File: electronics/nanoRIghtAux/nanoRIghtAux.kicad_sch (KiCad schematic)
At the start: 18 parts, among them J1 Conn_MM5451, J10 Conn_EA_GLCD, J11 Conn_MAX7219, J12 Conn_PWRInput, J13 Conn_MAX_Pwr, J2 Conn_HYDA, J3 Conn_HYDB, J4 Conn_FUEL_FR, J5 Conn_FUEL_AL, J6 Conn_MOT_D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

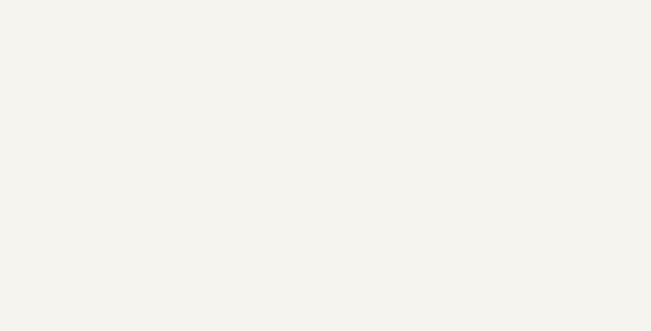
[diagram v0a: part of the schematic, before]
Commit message: mountingholes addes
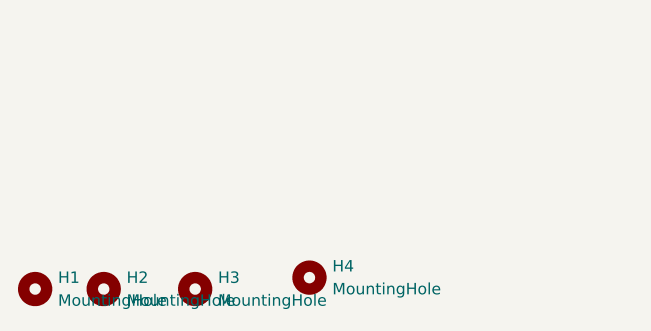
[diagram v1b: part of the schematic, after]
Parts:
- added H1, H2, H3, H4: MountingHole, MountingHole:MountingHole_3.5mm, symbol Mechanical:MountingHole
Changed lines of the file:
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@@
     (effects (font (size 1.27 1.27)) (justify left bottom))
+  )
+  (symbol (lib_id "Mechanical:MountingHole") (at 39.37 187.96 0) (unit 1)
+    (in_bom yes) (on_board yes) (dnp no) (fields_autoplaced)
+    (property "Reference" "H3" (at 41.91 186.69 0)
+      (effects (font (size 1.27 1.27)) (justify left))
+    )
+    (property "Value" "MountingHole" (at 41.91 189.23 0)
+      (effects (font (size 1.27 1.27)) (justify left))
+    )
+    (property "Footprint" "MountingHole:MountingHole_3.5mm" (at 39.37 187.96 0)
+      (effects (font (size 1.27 1.27)) hide)
+    )
+    (property "Datasheet" "~" (at 39.37 187.96 0)
+      (effects (font (size 1.27 1.27)) hide)
+    )
+    (instances
+      (project "nanoRIghtAux"
+        (path "/36bd7c2a-95a7-4ab3-af81-512b588298f0"
+          (reference "H3") (unit 1)
+        )
+      )
+    )
   )
   (symbol (lib_id "power:+5V") (at 90.17 121.92 0) (mirror x) (unit 1)
@@
         (path "/36bd7c2a-95a7-4ab3-af81-512b588298f0"
           (reference "SW2") (unit 1)
+        )
+      )
+    )
+  )
+  (symbol (lib_id "Mechanical:MountingHole") (at 29.21 187.96 0) (unit 1)
+    (in_bom yes) (on_board yes) (dnp no) (fields_autoplaced)
+    (property "Reference" "H2" (at 31.75 186.69 0)
+      (effects (font (size 1.27 1.27)) (justify left))
+    )
+    (property "Value" "MountingHole" (at 31.75 189.23 0)
+      (effects (font (size 1.27 1.27)) (justify left))
+    )
+    (property "Footprint" "MountingHole:MountingHole_3.5mm" (at 29.21 187.96 0)
+      (effects (font (size 1.27 1.27)) hide)
+    )
+    (property "Datasheet" "~" (at 29.21 187.96 0)
+      (effects (font (size 1.27 1.27)) hide)
+    )
+    (instances
+      (project "nanoRIghtAux"
+        (path "/36bd7c2a-95a7-4ab3-af81-512b588298f0"
+          (reference "H2") (unit 1)
         )
       )
@@
         )
       )
+    )
+  )
+  (symbol (lib_id "Mechanical:MountingHole") (at 52.07 186.69 0) (unit 1)
+    (in_bom yes) (on_board yes) (dnp no) (fields_autoplaced)
+    (property "Reference" "H4" (at 54.61 185.42 0)
+      (effects (font (size 1.27 1.27)) (justify left))
+    )
+    (property "Value" "MountingHole" (at 54.61 187.96 0)
+      (effects (font (size 1.27 1.27)) (justify left))
+    )
+    (property "Footprint" "MountingHole:MountingHole_3.5mm" (at 52.07 186.69 0)
+      (effects (font (size 1.27 1.27)) hide)
+    )
+    (property "Datasheet" "~" (at 52.07 186.69 0)
+      (effects (font (size 1.27 1.27)) hide)
+    )
+    (instances
+      (project "nanoRIghtAux"
+        (path "/36bd7c2a-95a7-4ab3-af81-512b588298f0"
+          (reference "H4") (unit 1)
+        )
+      )
+    )
+  )
+  (symbol (lib_id "Mechanical:MountingHole") (at 21.59 187.96 0) (unit 1)
+    (in_bom yes) (on_board yes) (dnp no) (fields_autoplaced)
+    (property "Reference" "H1" (at 24.13 186.69 0)
+      (effects (font (size 1.27 1.27)) (justify left))
+    )
+    (property "Value" "MountingHole" (at 24.13 189.23 0)
+      (effects (font (size 1.27 1.27)) (justify left))
+    )
+    (property "Footprint" "MountingHole:MountingHole_3.5mm" (at 21.59 187.96 0)
+      (effects (font (size 1.27 1.27)) hide)
+    )
+    (property "Datasheet" "~" (at 21.59 187.96 0)
+      (effects (font (size 1.27 1.27)) hide)
+    )
+    (instances
+      (project "nanoRIghtAux"
+        (path "/36bd7c2a-95a7-4ab3-af81-512b588298f0"
+          (reference "H1") (unit 1)
+        )
+      )

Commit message: changed footprint of AX12 to DIP28
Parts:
- U3: footprint Package_SO:SOIC-28W_7.5x17.9mm_P1.27mm -> Package_DIP:DIP-28_W15.24mm
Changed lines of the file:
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@@
       (effects (font (size 1.27 1.27)) (justify left))
     )
-    (property "Footprint" "Package_SO:SOIC-28W_7.5x17.9mm_P1.27mm" (at 220.98 96.52 0)
+    (property "Footprint" "Package_DIP:DIP-28_W15.24mm" (at 220.98 96.52 0)
       (effects (font (size 1.27 1.27)) hide)
     )

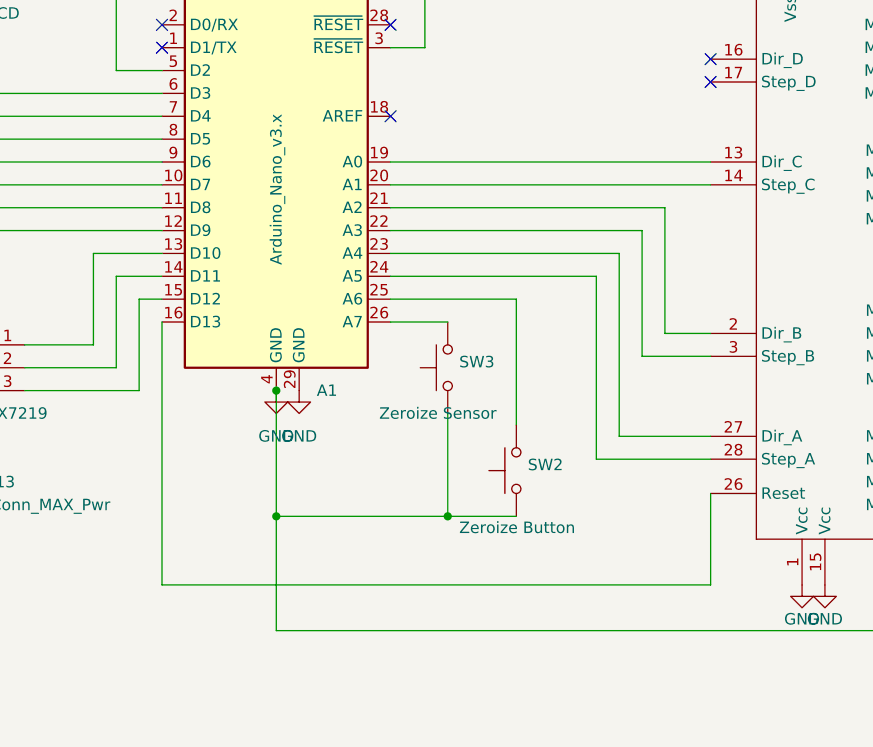
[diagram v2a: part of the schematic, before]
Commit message: changed pin assignments for AX12 to facilitate routing
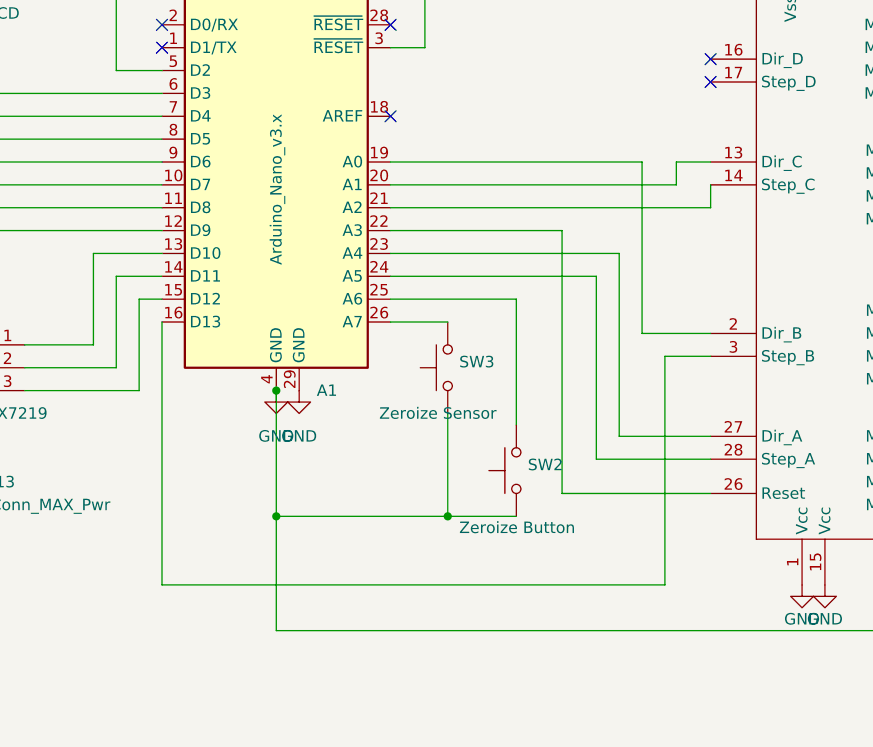
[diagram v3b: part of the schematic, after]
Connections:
- net at U3.13 (Dir_C): now also A1.20 (A1); no longer A1.19 (A0)
- net at U3.14 (Step_C): now also A1.21 (A2); no longer A1.20 (A1)
- net at U3.2 (Dir_B): now also A1.19 (A0); no longer A1.21 (A2)
- net at U3.26 (Reset): now also A1.22 (A3); no longer A1.16 (D13)
- net at U3.3 (Step_B): now also A1.16 (D13); no longer A1.22 (A3)
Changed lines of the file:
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@@
+    (stroke (width 0) (type default))
+  )
+  (wire (pts (xy 201.93 106.68) (xy 207.01 106.68))
     (stroke (width 0) (type default))
   )
@@
     (stroke (width 0) (type default))
   )
+  (wire (pts (xy 201.93 132.08) (xy 201.93 106.68))
+    (stroke (width 0) (type default))
+  )
   (wire (pts (xy 241.3 123.19) (xy 236.22 123.19))
     (stroke (width 0) (type default))
@@
     (stroke (width 0) (type default))
   )
-  (wire (pts (xy 171.45 92.71) (xy 199.39 92.71))
+  (wire (pts (xy 171.45 92.71) (xy 190.5 92.71))
+    (stroke (width 0) (type default))
+  )
+  (wire (pts (xy 190.5 92.71) (xy 190.5 121.92))
     (stroke (width 0) (type default))
   )
@@
     (stroke (width 0) (type default))
   )
+  (wire (pts (xy 190.5 121.92) (xy 207.01 121.92))
+    (stroke (width 0) (type default))
+  )
   (wire (pts (xy 241.3 77.47) (xy 236.22 77.47))
     (stroke (width 0) (type default))
@@
     (stroke (width 0) (type default))
   )
-  (wire (pts (xy 171.45 87.63) (xy 207.01 87.63))
-    (stroke (width 0) (type default))
-  )
   (wire (pts (xy 143.51 100.33) (xy 143.51 110.49))
     (stroke (width 0) (type default))
@@
     (stroke (width 0) (type default))
   )
-  (wire (pts (xy 171.45 85.09) (xy 207.01 85.09))
-    (stroke (width 0) (type default))
-  )
-  (wire (pts (xy 199.39 92.71) (xy 199.39 106.68))
-    (stroke (width 0) (type default))
-  )
   (wire (pts (xy 146.05 87.63) (xy 100.33 87.63))
     (stroke (width 0) (type default))
@@
     (stroke (width 0) (type default))
   )
-  (wire (pts (xy 171.45 90.17) (xy 201.93 90.17))
+  (wire (pts (xy 171.45 87.63) (xy 203.2 87.63))
     (stroke (width 0) (type default))
   )
@@
     (stroke (width 0) (type default))
   )
-  (wire (pts (xy 201.93 104.14) (xy 207.01 104.14))
-    (stroke (width 0) (type default))
-  )
   (wire (pts (xy 58.42 82.55) (xy 58.42 92.71))
     (stroke (width 0) (type default))
@@
     (stroke (width 0) (type default))
   )
+  (wire (pts (xy 203.2 87.63) (xy 203.2 85.09))
+    (stroke (width 0) (type default))
+  )
   (wire (pts (xy 236.22 69.85) (xy 236.22 71.12))
     (stroke (width 0) (type default))
@@
     (stroke (width 0) (type default))
   )
+  (wire (pts (xy 199.39 104.14) (xy 199.39 85.09))
+    (stroke (width 0) (type default))
+  )
   (wire (pts (xy 171.45 97.79) (xy 194.31 97.79))
     (stroke (width 0) (type default))
@@
     (stroke (width 0) (type default))
   )
-  (wire (pts (xy 146.05 132.08) (xy 207.01 132.08))
+  (wire (pts (xy 171.45 90.17) (xy 207.01 90.17))
+    (stroke (width 0) (type default))
+  )
+  (wire (pts (xy 146.05 132.08) (xy 201.93 132.08))
     (stroke (width 0) (type default))
   )
@@
     (stroke (width 0) (type default))
   )
-  (wire (pts (xy 207.01 132.08) (xy 207.01 121.92))
-    (stroke (width 0) (type default))
-  )
   (wire (pts (xy 236.22 104.14) (xy 238.76 104.14))
     (stroke (width 0) (type default))
   )
+  (wire (pts (xy 199.39 85.09) (xy 171.45 85.09))
+    (stroke (width 0) (type default))
+  )
   (wire (pts (xy 236.22 101.6) (xy 236.22 102.87))
     (stroke (width 0) (type default))
@@
     (stroke (width 0) (type default))
   )
-  (wire (pts (xy 201.93 90.17) (xy 201.93 104.14))
-    (stroke (width 0) (type default))
-  )
   (wire (pts (xy 236.22 83.82) (xy 236.22 85.09))
     (stroke (width 0) (type default))
@@
     (stroke (width 0) (type default))
   )
-  (wire (pts (xy 199.39 106.68) (xy 207.01 106.68))
+  (wire (pts (xy 207.01 104.14) (xy 199.39 104.14))
     (stroke (width 0) (type default))
   )
@@
     (stroke (width 0) (type default))
   )
+  (wire (pts (xy 207.01 90.17) (xy 207.01 87.63))
+    (stroke (width 0) (type default))
+  )
   (wire (pts (xy 105.41 139.7) (xy 92.71 139.7))
     (stroke (width 0) (type default))
   )
+  (wire (pts (xy 203.2 85.09) (xy 207.01 85.09))
+    (stroke (width 0) (type default))
+  )

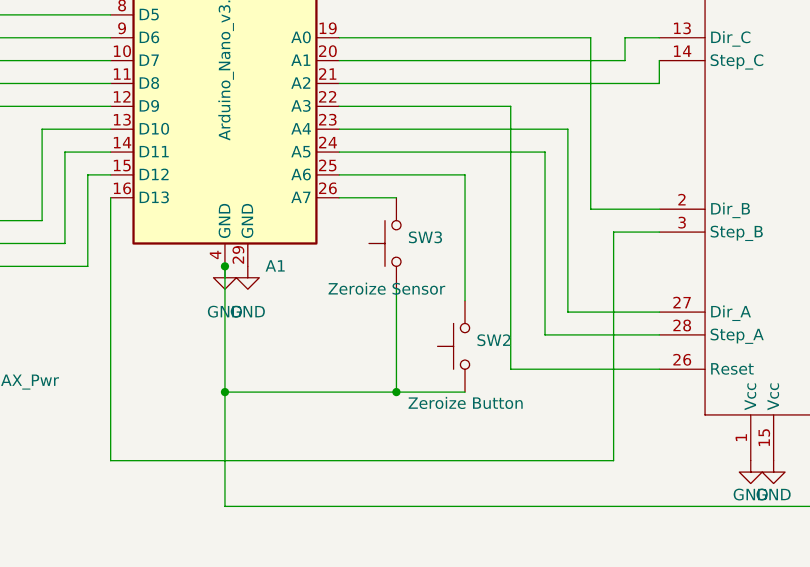
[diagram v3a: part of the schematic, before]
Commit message: more routing added
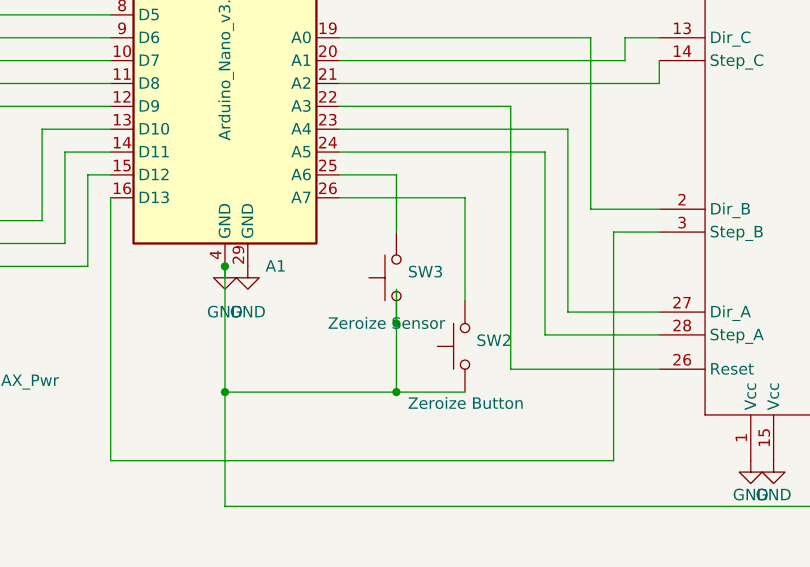
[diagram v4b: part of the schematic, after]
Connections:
- net at SW2.2: now also A1.26 (A7); no longer A1.25 (A6)
- net at SW3.2: now also A1.25 (A6); no longer A1.26 (A7)
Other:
- moved on the sheet: SW3
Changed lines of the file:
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@@
   (junction (at 35.56 26.67) (diameter 0) (color 0 0 0 0)
+  )
+  (junction (at 177.8 116.84) (diameter 0) (color 0 0 0 0)
   )
   (junction (at 109.22 60.96) (diameter 0) (color 0 0 0 0)
@@
     (stroke (width 0) (type default))
   )
+  (wire (pts (xy 171.45 100.33) (xy 177.8 100.33))
+    (stroke (width 0) (type default))
+  )
   (wire (pts (xy 140.97 60.96) (xy 140.97 74.93))
     (stroke (width 0) (type default))
@@
     (stroke (width 0) (type default))
   )
+  (wire (pts (xy 177.8 116.84) (xy 177.8 124.46))
+    (stroke (width 0) (type default))
+  )
   (wire (pts (xy 171.45 92.71) (xy 190.5 92.71))
     (stroke (width 0) (type default))
@@
     (stroke (width 0) (type default))
   )
-  (wire (pts (xy 171.45 102.87) (xy 177.8 102.87))
+  (wire (pts (xy 171.45 102.87) (xy 185.42 102.87))
     (stroke (width 0) (type default))
   )
@@
     (stroke (width 0) (type default))
   )
+  (wire (pts (xy 177.8 100.33) (xy 177.8 106.68))
+    (stroke (width 0) (type default))
+  )
   (wire (pts (xy 199.39 85.09) (xy 171.45 85.09))
     (stroke (width 0) (type default))
@@
     (stroke (width 0) (type default))
   )
-  (wire (pts (xy 185.42 114.3) (xy 185.42 100.33))
+  (wire (pts (xy 185.42 114.3) (xy 185.42 102.87))
     (stroke (width 0) (type default))
   )
@@
     (stroke (width 0) (type default))
   )
-  (wire (pts (xy 177.8 113.03) (xy 177.8 124.46))
+  (wire (pts (xy 177.8 113.03) (xy 177.8 116.84))
     (stroke (width 0) (type default))
   )
@@
   )
   (wire (pts (xy 241.3 109.22) (xy 236.22 109.22))
-    (stroke (width 0) (type default))
-  )
-  (wire (pts (xy 185.42 100.33) (xy 171.45 100.33))
     (stroke (width 0) (type default))
   )
@@
     )
   )
-  (symbol (lib_id "Switch:SW_Push") (at 177.8 107.95 90) (unit 1)
-    (in_bom yes) (on_board yes) (dnp no)
-    (property "Reference" "SW3" (at 179.07 107.315 90)
+  (symbol (lib_id "Switch:SW_Push") (at 177.8 111.76 90) (unit 1)
+    (in_bom yes) (on_board yes) (dnp no)
+    (property "Reference" "SW3" (at 179.07 111.125 90)
       (effects (font (size 1.27 1.27)) (justify right))
     )
-    (property "Value" "Zeroize Sensor" (at 170.18 113.03 90)
+    (property "Value" "Zeroize Sensor" (at 170.18 116.84 90)
       (effects (font (size 1.27 1.27)) (justify right))
     )
-    (property "Footprint" "Connector_PinHeader_2.54mm:PinHeader_1x02_P2.54mm_Vertical" (at 172.72 107.95 0)
-      (effects (font (size 1.27 1.27)) hide)
-    )
-    (property "Datasheet" "~" (at 172.72 107.95 0)
-      (effects (font (size 1.27 1.27)) hide)
-    )
+    (property "Footprint" "Connector_PinHeader_2.54mm:PinHeader_1x02_P2.54mm_Vertical" (at 172.72 111.76 0)
+      (effects (font (size 1.27 1.27)) hide)
+    )
+    (property "Datasheet" "~" (at 172.72 111.76 0)
+      (effects (font (size 1.27 1.27)) hide)
+    )

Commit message: routing done
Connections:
- net at U3.27 (Dir_A): now also A1.24 (A5); no longer A1.23 (A4)
- net at U3.28 (Step_A): now also A1.23 (A4); no longer A1.24 (A5)
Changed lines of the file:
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@@
     (stroke (width 0) (type default))
   )
-  (wire (pts (xy 194.31 97.79) (xy 194.31 118.11))
+  (wire (pts (xy 194.31 97.79) (xy 194.31 115.57))
     (stroke (width 0) (type default))
   )
@@
     (stroke (width 0) (type default))
   )
-  (wire (pts (xy 196.85 115.57) (xy 207.01 115.57))
-    (stroke (width 0) (type default))
-  )
   (wire (pts (xy 190.5 121.92) (xy 207.01 121.92))
     (stroke (width 0) (type default))
@@
     (stroke (width 0) (type default))
   )
-  (wire (pts (xy 194.31 118.11) (xy 207.01 118.11))
-    (stroke (width 0) (type default))
-  )
   (wire (pts (xy 41.91 26.67) (xy 46.99 26.67))
     (stroke (width 0) (type default))
@@
     (stroke (width 0) (type default))
   )
+  (wire (pts (xy 196.85 118.11) (xy 207.01 118.11))
+    (stroke (width 0) (type default))
+  )
   (wire (pts (xy 171.45 102.87) (xy 185.42 102.87))
     (stroke (width 0) (type default))
@@
     (stroke (width 0) (type default))
   )
+  (wire (pts (xy 194.31 115.57) (xy 207.01 115.57))
+    (stroke (width 0) (type default))
+  )
   (wire (pts (xy 241.3 115.57) (xy 241.3 116.84))
     (stroke (width 0) (type default))
@@
     (stroke (width 0) (type default))
   )
-  (wire (pts (xy 196.85 95.25) (xy 196.85 115.57))
-    (stroke (width 0) (type default))
-  )
+  (wire (pts (xy 196.85 95.25) (xy 196.85 118.11))
+    (stroke (width 0) (type default))
+  )
